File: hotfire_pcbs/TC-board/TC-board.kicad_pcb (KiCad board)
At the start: 2 copper layers, 70.1 x 69.6 mm, 15 parts, among them J1 DB15_Female, J3 PCIE-LP-01-01-F-DV-A-TR, U1 MAX31856_Breakout, U2 MAX31856_Breakout

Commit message: TC Board (Updated March 19th)
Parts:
- CS_0: renamed from TP8; value TestPoint -> CS_0; moved to F.Cu
- CS_1: renamed from TP9; value TestPoint -> CS_1
- MISO: renamed from TP5; value TestPoint -> MISO
- MOSI: renamed from TP6; value TestPoint -> MOSI
- SCK: renamed from TP7; value TestPoint -> SCK
- TC1_T+: renamed from TP2; value TestPoint -> T+
- TC1_T-: renamed from TP1; value TestPoint -> T-
- TC2_T+: renamed from TP4; value TestPoint -> T+
- TC2_T-: renamed from TP3; value TestPoint -> T-
- turned CS_0 to 0 degrees
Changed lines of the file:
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@@
     (property "Sheetname" "")
     (attr through_hole)
-    (fp_text reference "TP2" (at 0 -2.75) (layer "F.SilkS")
+    (fp_text reference "TC1_T+" (at -0.889 -2.75) (layer "F.SilkS")
       (effects (font (size 1 1) (thickness 0.15)))
     )
-    (fp_text value "TestPoint" (at -0.889 2.75) (layer "F.Fab")
+    (fp_text value "T+" (at -0.889 2.75) (layer "F.Fab")
       (effects (font (size 1 1) (thickness 0.15)))
     )
@@
     (property "Sheetname" "")
     (attr through_hole)
-    (fp_text reference "TP6" (at 0 -2.75) (layer "F.SilkS")
+    (fp_text reference "MOSI" (at 0 -2.75) (layer "F.SilkS")
       (effects (font (size 1 1) (thickness 0.15)))
     )
-    (fp_text value "TestPoint" (at 0 2.75) (layer "F.Fab")
+    (fp_text value "MOSI" (at 0 2.75) (layer "F.Fab")
       (effects (font (size 1 1) (thickness 0.15)))
     )
@@
     (property "Sheetname" "")
     (attr through_hole)
-    (fp_text reference "TP4" (at 0 -2.75) (layer "F.SilkS")
+    (fp_text reference "TC2_T+" (at -0.127 -2.921) (layer "F.SilkS")
       (effects (font (size 1 1) (thickness 0.15)))
     )
-    (fp_text value "TestPoint" (at -0.635 2.75) (layer "F.Fab")
+    (fp_text value "T+" (at -0.635 2.75) (layer "F.Fab")
       (effects (font (size 1 1) (thickness 0.15)))
     )
@@
     (property "Sheetname" "")
     (attr through_hole)
-    (fp_text reference "TP5" (at 0 -2.75) (layer "F.SilkS")
+    (fp_text reference "MISO" (at 0 -2.75) (layer "F.SilkS")
       (effects (font (size 1 1) (thickness 0.15)))
     )
-    (fp_text value "TestPoint" (at 0 2.75) (layer "F.Fab")
+    (fp_text value "MISO" (at 0 2.75) (layer "F.Fab")
       (effects (font (size 1 1) (thickness 0.15)))
     )
@@
   )
   (footprint "TestPoint:TestPoint_Keystone_5010-5014_Multipurpose" (layer "F.Cu")
+    (at 224.282 121.158)
+    (descr "Keystone Miniature THM Test Point 5010-5014, http://www.keyelco.com/product-pdf.cfm?p=1319")
+    (tags "Through Hole Mount Test Points")
+    (property "Sheetfile" "TC-board.kicad_sch")
+    (property "Sheetname" "")
+    (attr through_hole)
+    (fp_text reference "CS_0" (at 0 -2.75) (layer "F.SilkS")
+      (effects (font (size 1 1) (thickness 0.15)))
+    )
+    (fp_text value "CS_0" (at 0 2.75) (layer "F.Fab")
+      (effects (font (size 1 1) (thickness 0.15)))
+    )
+    (fp_text user "${REFERENCE}" (at 0 0) (layer "F.Fab")
+      (effects (font (size 0.6 0.6) (thickness 0.09)))
+    )
+    (fp_circle (center 0 0) (end 1.75 0) (layer "F.SilkS") (width 0.15) (fill none))
+    (fp_circle (center 0 0) (end 2 0) (layer "F.CrtYd") (width 0.05) (fill none))
+    (fp_line (start -1.25 0.4) (end -1.25 -0.4) (layer "F.Fab") (width 0.15))
+    (fp_line (start 1.25 0.4) (end -1.25 0.4) (layer "F.Fab") (width 0.15))
+    (fp_line (start -1.25 -0.4) (end 1.25 -0.4) (layer "F.Fab") (width 0.15))
+    (fp_line (start 1.25 -0.4) (end 1.25 0.4) (layer "F.Fab") (width 0.15))
+    (fp_circle (center 0 0) (end 1.6 0) (layer "F.Fab") (width 0.15) (fill none))
+    (pad "1" thru_hole circle (at 0 0) (size 2.8 2.8) (drill 1.6) (layers *.Cu *.Mask)
+      (net 21 "/SPI_CS_0") (pinfunction "1") (pintype "passive"))
+    (model "${KICAD6_3DMODEL_DIR}/TestPoint.3dshapes/TestPoint_Keystone_5010-5014_Multipurpose.wrl"
+      (offset (xyz 0 0 0))
+      (scale (xyz 1 1 1))
+      (rotate (xyz 0 0 0))
+    )
+  )
+  (footprint "TestPoint:TestPoint_Keystone_5010-5014_Multipurpose" (layer "F.Cu")
     (at 217.17 121.158)
     (descr "Keystone Miniature THM Test Point 5010-5014, http://www.keyelco.com/product-pdf.cfm?p=1319")
@@
     (property "Sheetname" "")
     (attr through_hole)
-    (fp_text reference "TP7" (at 0 -2.75) (layer "F.SilkS")
+    (fp_text reference "SCK" (at 0 -2.75) (layer "F.SilkS")
       (effects (font (size 1 1) (thickness 0.15)))
     )
-    (fp_text value "TestPoint" (at 0 2.75) (layer "F.Fab")
+    (fp_text value "SCK" (at 0 2.75) (layer "F.Fab")
       (effects (font (size 1 1) (thickness 0.15)))
     )
@@
     (property "Sheetname" "")
     (attr through_hole)
-    (fp_text reference "TP9" (at 0 -2.75) (layer "F.SilkS")
+    (fp_text reference "CS_1" (at 0 -2.75) (layer "F.SilkS")
       (effects (font (size 1 1) (thickness 0.15)))
     )
-    (fp_text value "TestPoint" (at 0 2.75) (layer "F.Fab")
+    (fp_text value "CS_1" (at 0 2.75) (layer "F.Fab")
       (effects (font (size 1 1) (thickness 0.15)))
     )
@@
     (property "Sheetname" "")
     (attr through_hole)
-    (fp_text reference "TP1" (at 0 -2.75) (layer "F.SilkS")
+    (fp_text reference "TC1_T-" (at 0.508 -2.794) (layer "F.SilkS")
       (effects (font (size 1 1) (thickness 0.15)))
     )
-    (fp_text value "TestPoint" (at 1.27 2.75) (layer "F.Fab")
+    (fp_text value "T-" (at 1.27 2.75) (layer "F.Fab")
       (effects (font (size 1 1) (thickness 0.15)))
     )
@@
     (property "Sheetname" "")
     (attr through_hole)
-    (fp_text reference "TP3" (at 0 -2.75) (layer "F.SilkS")
+    (fp_text reference "TC2_T-" (at 1.016 -2.921) (layer "F.SilkS")
       (effects (font (size 1 1) (thickness 0.15)))
     )
-    (fp_text value "TestPoint" (at 1.016 2.75) (layer "F.Fab")
+    (fp_text value "T-" (at 1.016 2.75) (layer "F.Fab")
       (effects (font (size 1 1) (thickness 0.15)))
     )
@@
       ) (layer "B.SilkS") (width 0) (fill solid))
   )
-  (footprint "TestPoint:TestPoint_Keystone_5010-5014_Multipurpose" (layer "B.Cu")
-    (at 224.282 121.158 180)
-    (descr "Keystone Miniature THM Test Point 5010-5014, http://www.keyelco.com/product-pdf.cfm?p=1319")
-    (tags "Through Hole Mount Test Points")
-    (property "Sheetfile" "TC-board.kicad_sch")
-    (property "Sheetname" "")
-    (attr through_hole)
-    (fp_text reference "TP8" (at 0 2.75) (layer "F.SilkS")
-      (effects (font (size 1 1) (thickness 0.15)))
-    )
-    (fp_text value "TestPoint" (at 0 -2.75) (layer "F.Fab")
-      (effects (font (size 1 1) (thickness 0.15)))
-    )
-    (fp_text user "${REFERENCE}" (at 0 0) (layer "B.Fab")
-      (effects (font (size 0.6 0.6) (thickness 0.09)) (justify mirror))
-    )
-    (fp_circle (center 0 0) (end 1.75 0) (layer "B.SilkS") (width 0.15) (fill none))
-    (fp_circle (center 0 0) (end 2 0) (layer "B.CrtYd") (width 0.05) (fill none))
-    (fp_line (start -1.25 -0.4) (end -1.25 0.4) (layer "B.Fab") (width 0.15))
-    (fp_line (start 1.25 -0.4) (end -1.25 -0.4) (layer "B.Fab") (width 0.15))
-    (fp_line (start -1.25 0.4) (end 1.25 0.4) (layer "B.Fab") (width 0.15))
-    (fp_line (start 1.25 0.4) (end 1.25 -0.4) (layer "B.Fab") (width 0.15))
-    (fp_circle (center 0 0) (end 1.6 0) (layer "B.Fab") (width 0.15) (fill none))
-    (pad "1" thru_hole circle (at 0 0 180) (size 2.8 2.8) (drill 1.6) (layers *.Cu *.Mask)
-      (net 21 "/SPI_CS_0") (pinfunction "1") (pintype "passive"))
-    (model "${KICAD6_3DMODEL_DIR}/TestPoint.3dshapes/TestPoint_Keystone_5010-5014_Multipurpose.wrl"
-      (offset (xyz 0 0 0))
-      (scale (xyz 1 1 1))
-      (rotate (xyz 0 0 0))
-    )
-  )
   (gr_line (start 235.16 59.906) (end 235.194 129.531) (layer "Edge.Cuts") (width 0.1))

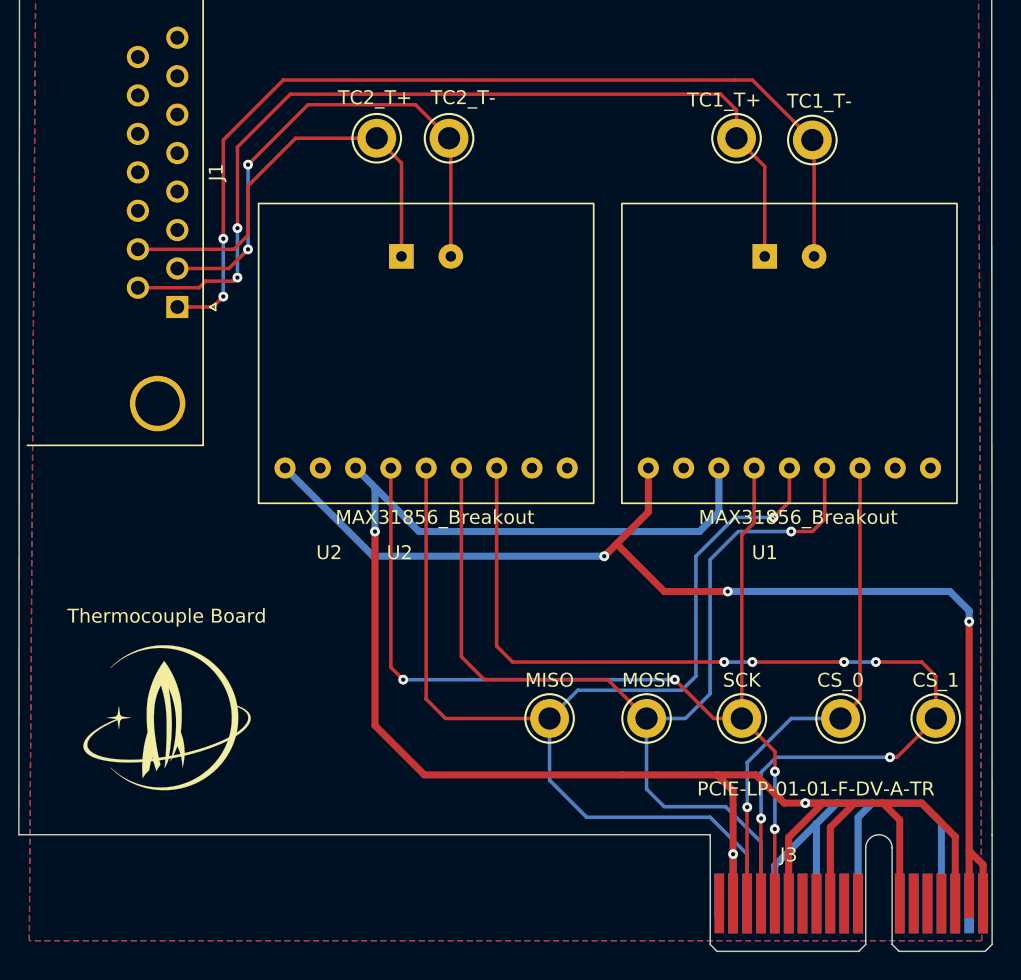
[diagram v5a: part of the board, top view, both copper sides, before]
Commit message: Fixed card edge clearance violation
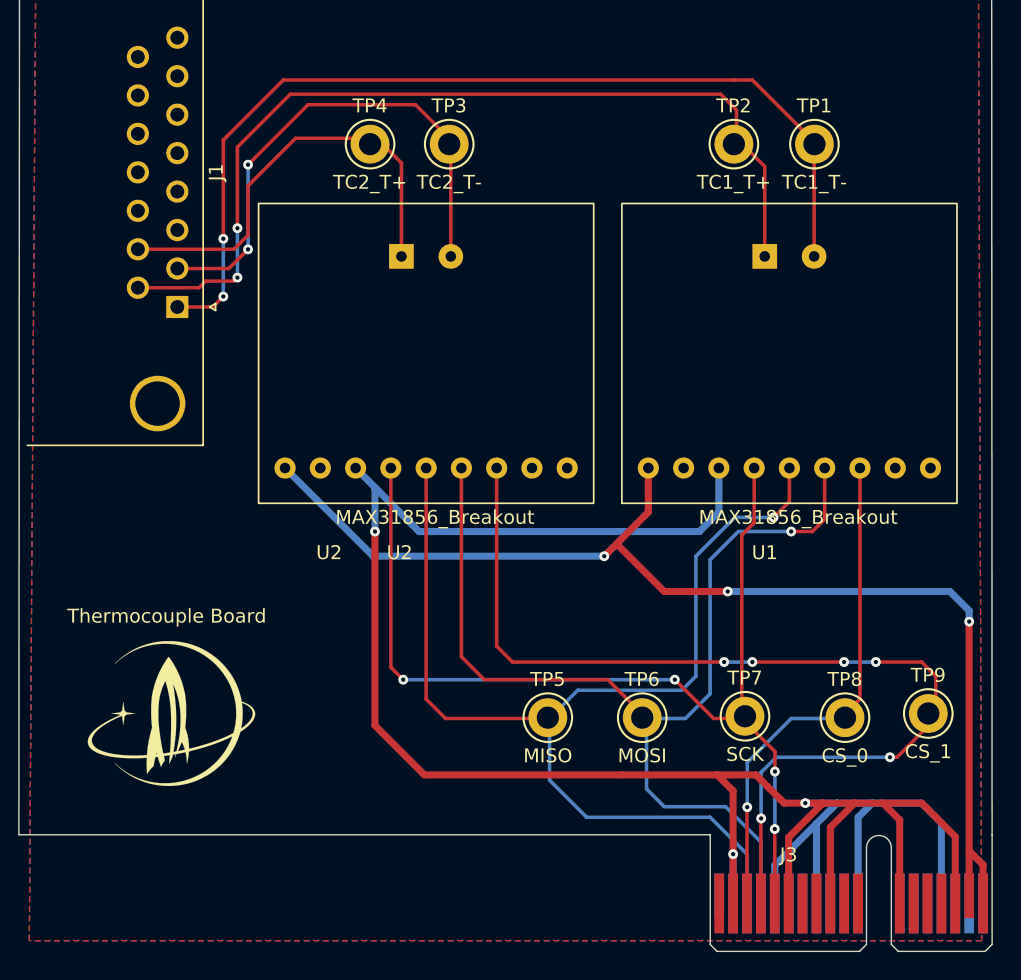
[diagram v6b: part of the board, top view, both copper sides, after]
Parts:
- removed CS_0: CS_0, TestPoint:TestPoint_Keystone_5010-5014_Multipurpose
- removed CS_1: CS_1, TestPoint:TestPoint_Keystone_5010-5014_Multipurpose
- removed MISO: MISO, TestPoint:TestPoint_Keystone_5010-5014_Multipurpose
- removed MOSI: MOSI, TestPoint:TestPoint_Keystone_5010-5014_Multipurpose
- removed SCK: SCK, TestPoint:TestPoint_Keystone_5010-5014_Multipurpose
- removed TC1_T+, TC2_T+: T+, TestPoint:TestPoint_Keystone_5010-5014_Multipurpose
- removed TC1_T-, TC2_T-: T-, TestPoint:TestPoint_Keystone_5010-5014_Multipurpose
- added TP1: TC1_T-, TestPoint:TestPoint_Keystone_5010-5014_Multipurpose, F.Cu at (222.4, 79.8)
- added TP2: TC1_T+, TestPoint:TestPoint_Keystone_5010-5014_Multipurpose, F.Cu at (216.6, 79.8)
- added TP3: TC2_T-, TestPoint:TestPoint_Keystone_5010-5014_Multipurpose, F.Cu at (196.1, 79.8)
- added TP4: TC2_T+, TestPoint:TestPoint_Keystone_5010-5014_Multipurpose, F.Cu at (190.4, 79.8)
- added TP5: MISO, TestPoint:TestPoint_Keystone_5010-5014_Multipurpose, F.Cu at (203.2, 121.1)
- added TP6: MOSI, TestPoint:TestPoint_Keystone_5010-5014_Multipurpose, F.Cu at (210.0, 121.1)
- added TP7: SCK, TestPoint:TestPoint_Keystone_5010-5014_Multipurpose, F.Cu at (217.4, 121.0)
- added TP8: CS_0, TestPoint:TestPoint_Keystone_5010-5014_Multipurpose, F.Cu at (224.6, 121.1)
- added TP9: CS_1, TestPoint:TestPoint_Keystone_5010-5014_Multipurpose, F.Cu at (230.6, 120.8)
- J3: footprint Connector_PCBEdge:BUS_PCIexpress_x1 -> PCIe_x1_card_edge:PCIe_x1_card_edge
- moved G*** 0.44 mm to (176.1, 120.8)
